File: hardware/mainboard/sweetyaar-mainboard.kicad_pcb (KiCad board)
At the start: 4 copper layers, 80 x 80 mm, 102 parts

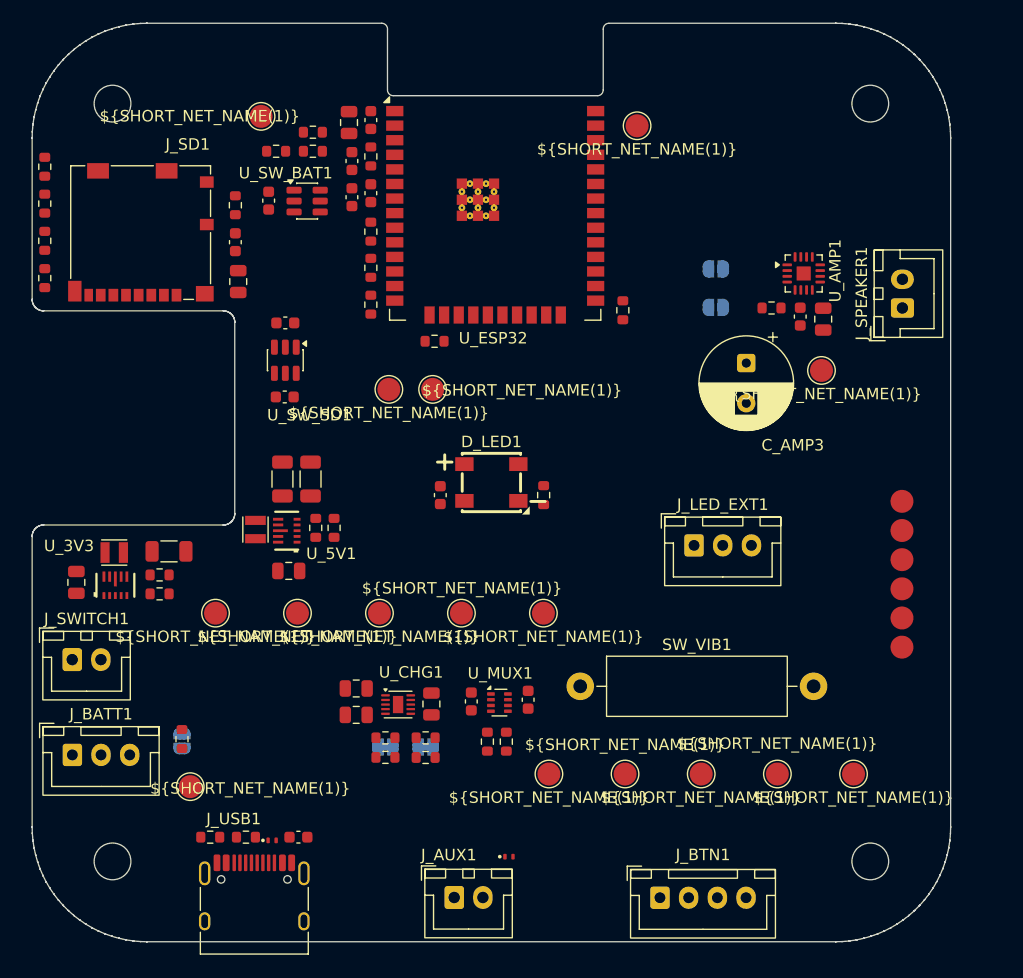
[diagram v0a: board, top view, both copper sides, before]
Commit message: Switch charger to firmware-supervised BQ25186
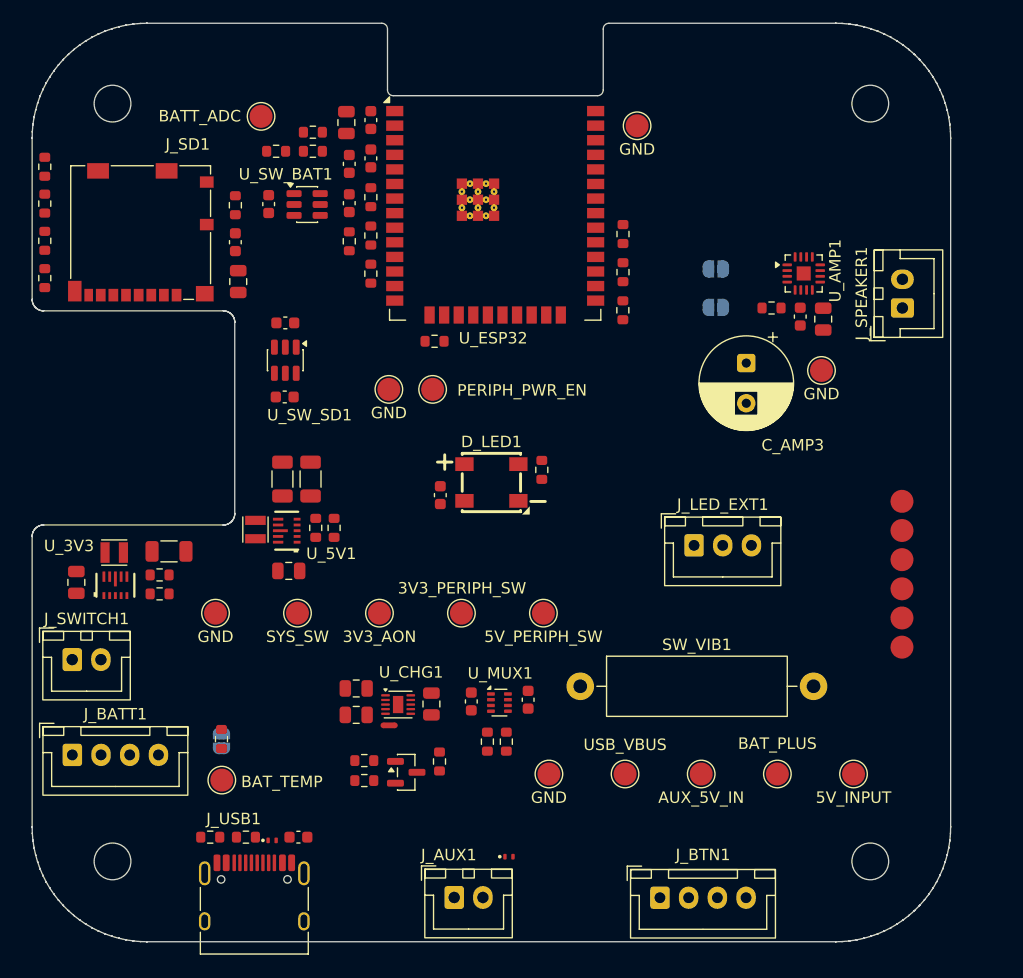
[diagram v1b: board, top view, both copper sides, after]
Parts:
- removed JP_ILIM1: JP_ILIM, Jumper:SolderJumper-2_P1.3mm_Bridged_RoundedPad1.0x1.5mm
- removed JP_ISET1: JP_ISET, Jumper:SolderJumper-2_P1.3mm_Bridged_RoundedPad1.0x1.5mm
- removed R_ILIM1: 5.1k, Resistor_SMD:R_0603_1608Metric
- removed R_ILIM2: 13k, Resistor_SMD:R_0603_1608Metric
- removed R_ISET1, R_ISET2: 301, Resistor_SMD:R_0603_1608Metric
- removed R_STAT1, R_STAT2: 10k, Resistor_SMD:R_0603_1608Metric
- added NT1: NetTie_2, NetTie:NetTie-2_SMD_Pad0.5mm, F.Cu at (51.1, 81.2)
- added Q1: MMBT3904, Package_TO_SOT_SMD:SOT-23, F.Cu at (52.6, 85.2)
- added R_CHARGER_CE_BASE1: 10k, Resistor_SMD:R_0603_1608Metric, F.Cu at (48.9, 84.2)
- added R_CHARGER_CE_PD1: 100k, Resistor_SMD:R_0603_1608Metric, F.Cu at (48.9, 86.0)
- added R_CHARGER_CE_PU1: 100k, Resistor_SMD:R_0603_1608Metric, F.Cu at (55.5, 84.3)
- added R_INT1: 10k, Resistor_SMD:R_0603_1608Metric, F.Cu at (49.5, 38.5)
- added R_PG1: 10k, Resistor_SMD:R_0603_1608Metric, F.Cu at (47.6, 39.0)
- added R_SCL1: 10k, Resistor_SMD:R_0603_1608Metric, F.Cu at (71.5, 38.4)
- added R_SDA1: 10k, Resistor_SMD:R_0603_1608Metric, F.Cu at (71.5, 41.7)
- J_BATT1: footprint Connector_JST:JST_XH_B3B-XH-A_1x03_P2.50mm_Vertical -> Connector_JST:JST_XH_B4B-XH-A_1x04_P2.50mm_Vertical
- TP1: value ${SHORT_NET_NAME(1)} -> USB_VBUS
- TP10: value ${SHORT_NET_NAME(1)} -> BATT_ADC
- TP11: value ${SHORT_NET_NAME(1)} -> BAT_TEMP
- TP12, TP13, TP14, TP15, TP16: value ${SHORT_NET_NAME(1)} -> GND
- TP2: value ${SHORT_NET_NAME(1)} -> AUX_5V_IN
- TP3: value ${SHORT_NET_NAME(1)} -> BAT_PLUS
- TP4: value ${SHORT_NET_NAME(1)} -> 5V_INPUT
- TP5: value ${SHORT_NET_NAME(1)} -> SYS_SW
- TP6: value ${SHORT_NET_NAME(1)} -> 5V_PERIPH_SW
- TP7: value ${SHORT_NET_NAME(1)} -> 3V3_PERIPH_SW
- TP8: value ${SHORT_NET_NAME(1)} -> 3V3_AON
- TP9: value ${SHORT_NET_NAME(1)} -> PERIPH_PWR_EN
- U_CHG1: value BQ25185DLHR -> BQ25186DLHR
- moved R_ESP_EN_PULLUP1 3.55 mm to (49.5, 35.1), turned to -90 degrees
- moved JP3 3.44 mm to (36.5, 82.5)
- moved R_TH1 3.44 mm to (36.5, 82.3)
- moved C_ESP_EN1 3.03 mm to (49.5, 31.8)
- moved TP11 2.81 mm to (36.5, 85.9)
- moved R_VIB1 2.70 mm to (49.5, 41.8)
- moved R_LED_DIN1 2.21 mm to (64.4, 58.9)
- moved C_BAT_SW_IN1 0.57 mm to (47.6, 35.7)
- moved C_BAT_ADC1 0.34 mm to (47.6, 32.2)
- moved U_SW_BAT1 0.30 mm to (44.0, 35.8)
- moved C_BAT_SW_OUT1 0.30 mm to (40.6, 35.8)
- moved C_ESP2 0.23 mm to (47.4, 28.6)
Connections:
- J_BATT1 pad 1: BAT_PLUS -> GND
- J_BATT1 pad 2: GND -> BAT_PLUS
- J_BATT1 pad 3: BAT_TEMP -> /TS_RETURN
- R_TH1 pad 2: GND -> /TS_RETURN
- U_CHG1 pad 3: /CHARGER_STAT2 -> /CHARGER_PG
- U_CHG1 pad 4: GND -> /CHARGER_CE_N
- U_CHG1 pad 7: /ILIM_VSET -> /I2C_SDA
- U_CHG1 pad 8: /ISET_NET -> /I2C_SCL
- U_CHG1 pad 9: /CHARGER_STAT1 -> /CHARGER_INT
- U_ESP32 pad 13: unconnected-(U_ESP32-IO14-Pad13) -> /CHARGER_ENABLE
- U_ESP32 pad 27: unconnected-(U_ESP32-IO16-Pad27) -> /I2C_SDA
- U_ESP32 pad 28: unconnected-(U_ESP32-IO17-Pad28) -> /I2C_SCL
- U_ESP32 pad 6: /CHARGER_STAT1 -> /CHARGER_PG
- U_ESP32 pad 7: /CHARGER_STAT2 -> /CHARGER_INT

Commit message: Adding routing to PCB design
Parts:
- removed C17: 10uF, 25V X5R/X7R, ±20%, Capacitor_SMD:C_0805_2012Metric
- removed C2: 22uF, 16 V, X5R/X7R, ±20%, Capacitor_SMD:C_1206_3216Metric
- removed TP12: GND, TestPoint:TestPoint_Pad_D2.0mm
- added C_3V3_OUT1: 22uF, 16 V, X5R/X7R, ±20%, Capacitor_SMD:C_1206_3216Metric, F.Cu at (31.1, 66.1)
- added C_5V_IN1: 10uF, 25V X5R/X7R, ±20%, Capacitor_SMD:C_0805_2012Metric, F.Cu at (48.2, 67.3)
- added C_MUX4: 1uF, 25 V, X7R, ±10%, Capacitor_SMD:C_0603_1608Metric, F.Cu at (52.7, 86.1)
- added LOGO: Logo_SweetYaar_Teddy_20x20mm, SweetYaar:Logo_SweetYaar_Teddy_20x20mm, F.Cu at (80.8, 83.5)
- moved TP3 46.5 mm to (38.5, 82.5)
- moved TP4 30.7 mm to (60.8, 85.4)
- moved TP15 18.4 mm to (69.4, 51.5)
- moved C_3V3_IN1 18.3 mm to (24.1, 69.0), turned to -90 degrees
- moved C_MUX1 14.7 mm to (46.6, 88.0), turned to 180 degrees
- moved C_MUX2 13.8 mm to (52.7, 87.9), turned to 0 degrees
- moved U_MUX1 13.8 mm to (49.6, 87.4)
- moved R_PR1_BOT1 13.1 mm to (50.2, 91.6)
- moved R_PR1_TOP1 13.1 mm to (51.8, 91.6)
- moved TP2 11.8 mm to (67.1, 89.4)
- moved TP1 11.5 mm to (60.8, 89.4)
- moved R_CHARGER_CE_PU1 10.6 mm to (64.4, 78.6)
- moved Q1 10.6 mm to (61.5, 79.5)
- moved R_CHARGER_CE_BASE1 10.6 mm to (57.9, 78.5)
- moved R_CHARGER_CE_PD1 10.6 mm to (57.9, 80.2)
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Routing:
- net GND: track 0.00 -> 136.3 mm, vias 0 -> 54
- net 3V3_AON: track 0.00 -> 117.7 mm, vias 0 -> 24
- net /ESP_EN: track 0.00 -> 106.4 mm, vias 0 -> 4
- net /BTN_SONG: track 0.00 -> 94.3 mm, vias 0 -> 2
- net /BTN_ANIMAL: track 0.00 -> 93.5 mm, vias 0 -> 2
- net BAT_PLUS: track 0.00 -> 87.3 mm, vias 0 -> 2
- net /UART_TXD: track 0.00 -> 84.2 mm
- net /UART_RXD: track 0.00 -> 79.3 mm
- net 3V3_PERIPH_SW: track 0.00 -> 70.9 mm, vias 0 -> 11
- net /SD_MOSI: track 0.00 -> 69.5 mm, vias 0 -> 4
- net /CHARGER_PG: track 0.00 -> 69.2 mm, vias 0 -> 2
- net /SD_CS: track 0.00 -> 68.8 mm, vias 0 -> 2
- net /BOOT: track 0.00 -> 67.7 mm
- net /SD_MISO: track 0.00 -> 65.2 mm, vias 0 -> 2
- net /SD_CLK: track 0.00 -> 59.7 mm, vias 0 -> 2
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- added copper zone on F.Cu, net /5V_INPUT
- added copper zone on F.Cu, net /SYS
- added copper zone on F.Cu, net /SYS_SW
- added copper zone on B.Cu, net 3V3_AON
- added copper zone on F.Cu, net 3V3_AON
- added copper zone on B.Cu, net 3V3_PERIPH_SW
- added copper zone on B.Cu, net 5V_PERIPH_SW
- added copper zone on F.Cu, net 5V_PERIPH_SW
- added copper zone on F.Cu, net BAT_PLUS
- added copper zone on F.Cu, net GND
- added copper zone on In1.Cu, net GND
- added copper zone on In2.Cu, net GND
- added copper zone on F.Cu, net Net-(U_3V3-L1)
- added copper zone on F.Cu, net Net-(U_3V3-L2)
- added copper zone on F.Cu, net Net-(U_5V1-L1)
- added copper zone on F.Cu, net Net-(U_5V1-L2)
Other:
- board text added: "Built with love by Zach Moshe for the world's cutest child ♥, 2022. Reimagined with Codex & Claude, 2026."
- board text added: "Close the jumper if no thermistor is connected to the battery harness. This connects a 10k resistor instead which the charger reads as a normal temperature."
- board text added: "High volume (12 dB)"
- board text added: "If both jumpers are open, volume is at a default level (9 dB). Close one of the jumpers to change settings. IMPORTANT: NEVER CLOSE BOTH!"
- board text added: "J_PROG1"
- board text added: "Low volume (6 dB)"

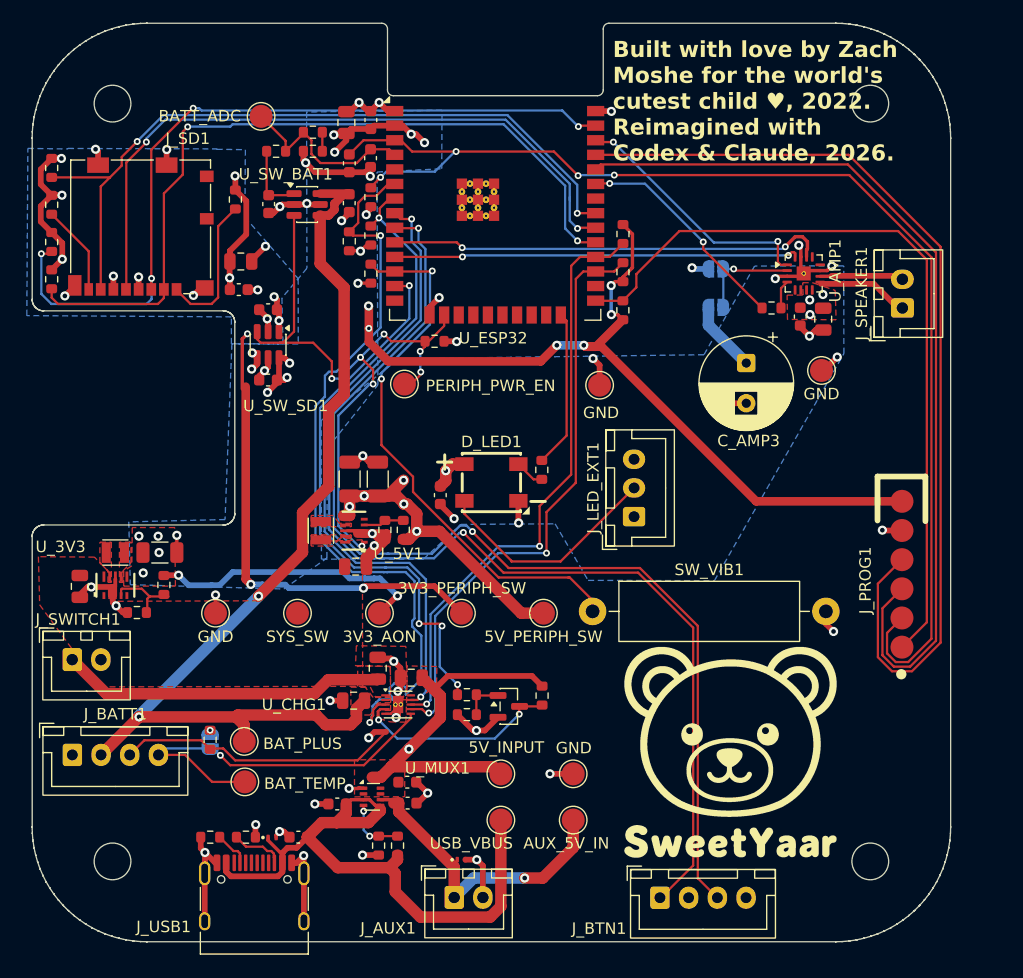
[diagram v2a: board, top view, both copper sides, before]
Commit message: Adding QR codes for repo and app; Adding version number to the silkscreen
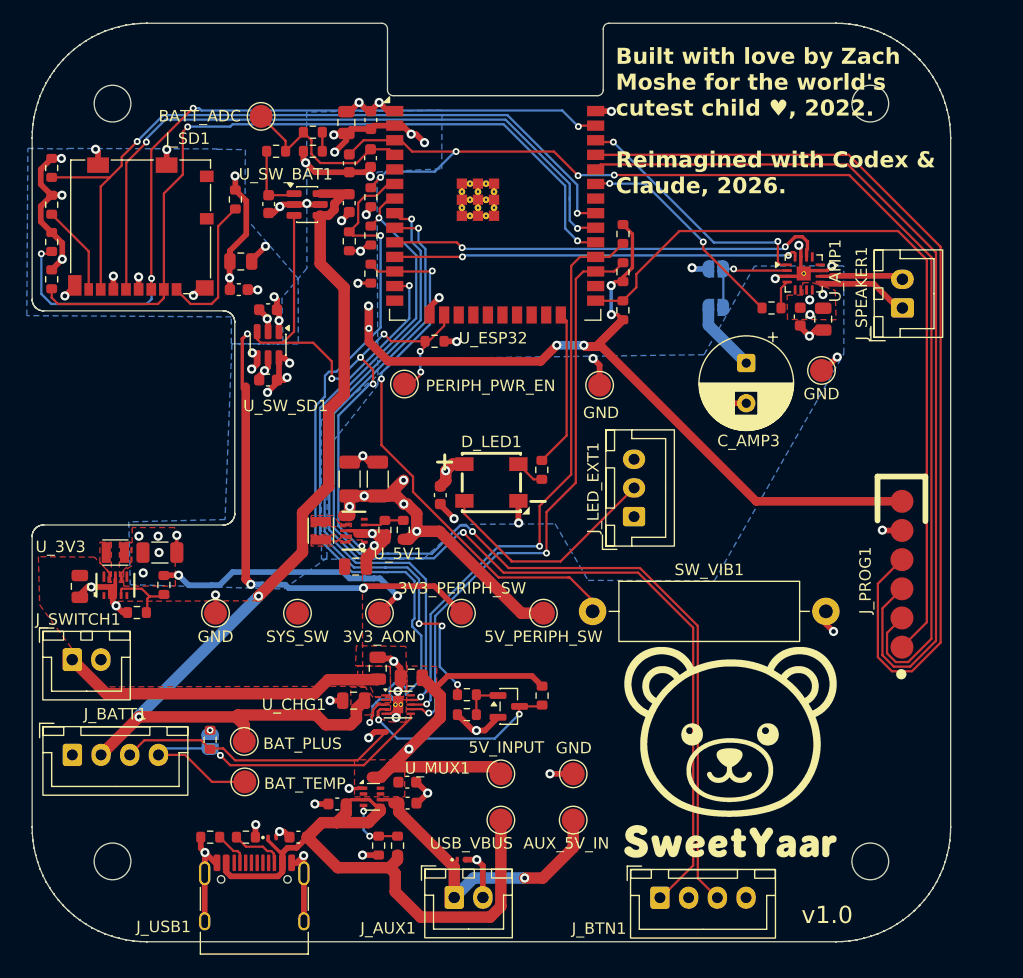
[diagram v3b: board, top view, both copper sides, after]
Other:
- board text added: "App"
- board text added: "Repo"
- board text added: "v1.0"

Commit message: Moving LED to the edge of the board
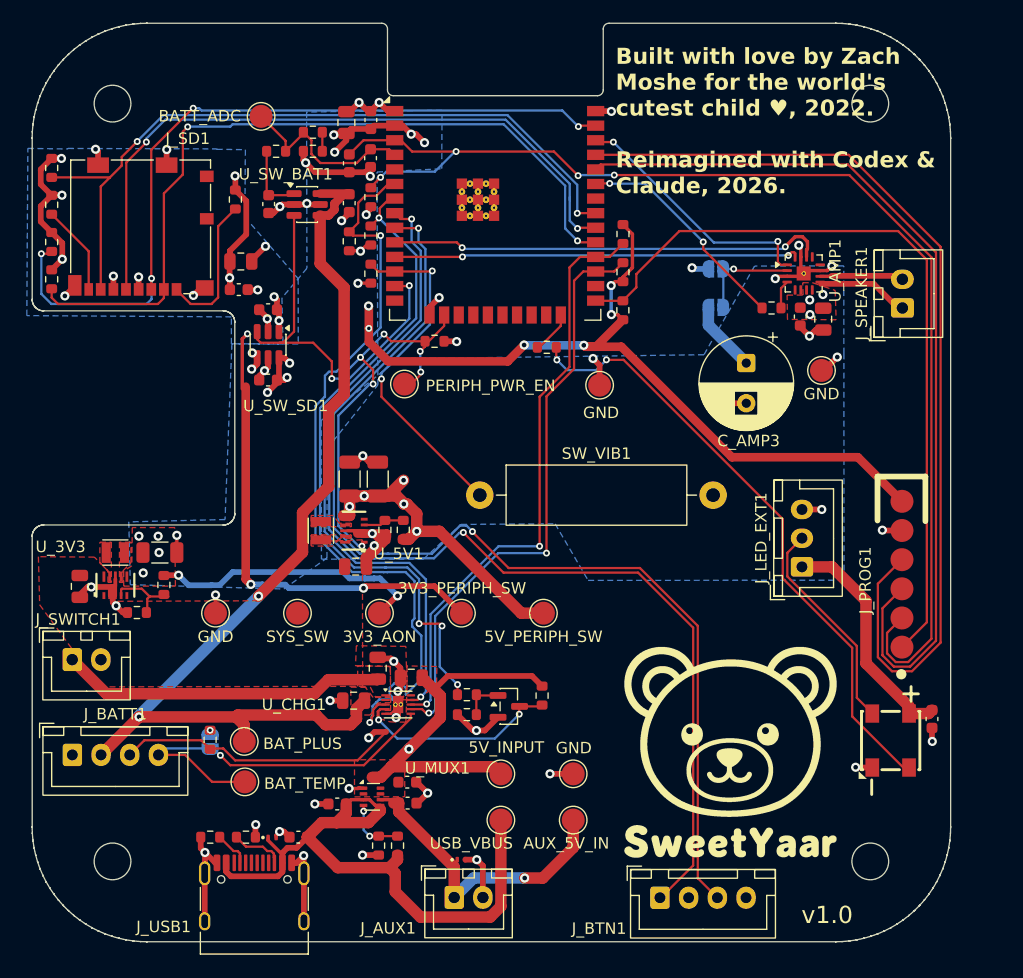
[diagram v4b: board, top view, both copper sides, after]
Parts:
- R_LED_DIN1: value 301 -> 330
- moved C_LED1 47.1 mm to (98.4, 80.6)
- moved D_LED1 41.4 mm to (94.8, 82.5), turned to -90 degrees
- moved J_LED_EXT1 15.3 mm to (87.0, 67.3)
- moved SW_VIB1 14.1 mm to (59.0, 61.1)
- moved R_LED_DIN1 10.7 mm to (64.8, 48.2), turned to 180 degrees
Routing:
- net Net-(D_LED1-DIN): track 2.59 -> 53.8 mm, vias 0 -> 2
- net /VIB_WAKE: track 48.4 -> 30.5 mm
- net 5V_PERIPH_SW: track 38.2 -> 55.1 mm, vias 9 -> 8
- net /STATUS_LED_GPIO: track 13.8 -> 4.27 mm
- net Net-(D_LED1-DOUT): track 20.3 -> 18.9 mm
- net GND: track 136.3 -> 134.9 mm

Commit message: Fixing rotation and position offsets
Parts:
- J_USB1: footprint SweetYaar:USB_C_Receptacle_HRO_TYPE-C-31-M-12 -> SweetYaar:USB_C_Receptacle_HRO_TYPE-C-31-M-12 - C165948
- U_AMP1: footprint SweetYaar:TQFN-16-1EP_3x3mm_P0.5mm_EP1.23x1.23mm -> SweetYaar:TQFN-16-1EP_3x3mm_P0.5mm_EP1.23x1.23mm - C910544
- U_ESP32: footprint RF_Module:ESP32-WROOM-32E -> SweetYaar:ESP32-WROOM-32E - C701342
- U_MUX1: footprint Package_TO_SOT_SMD:SOT-583-8 -> SweetYaar:SOT-583-8 - C3235557
- U_SW_BAT1, U_SW_SD1: footprint Package_TO_SOT_SMD:SOT-23-6 -> SweetYaar:SOT-23-6 - C128634

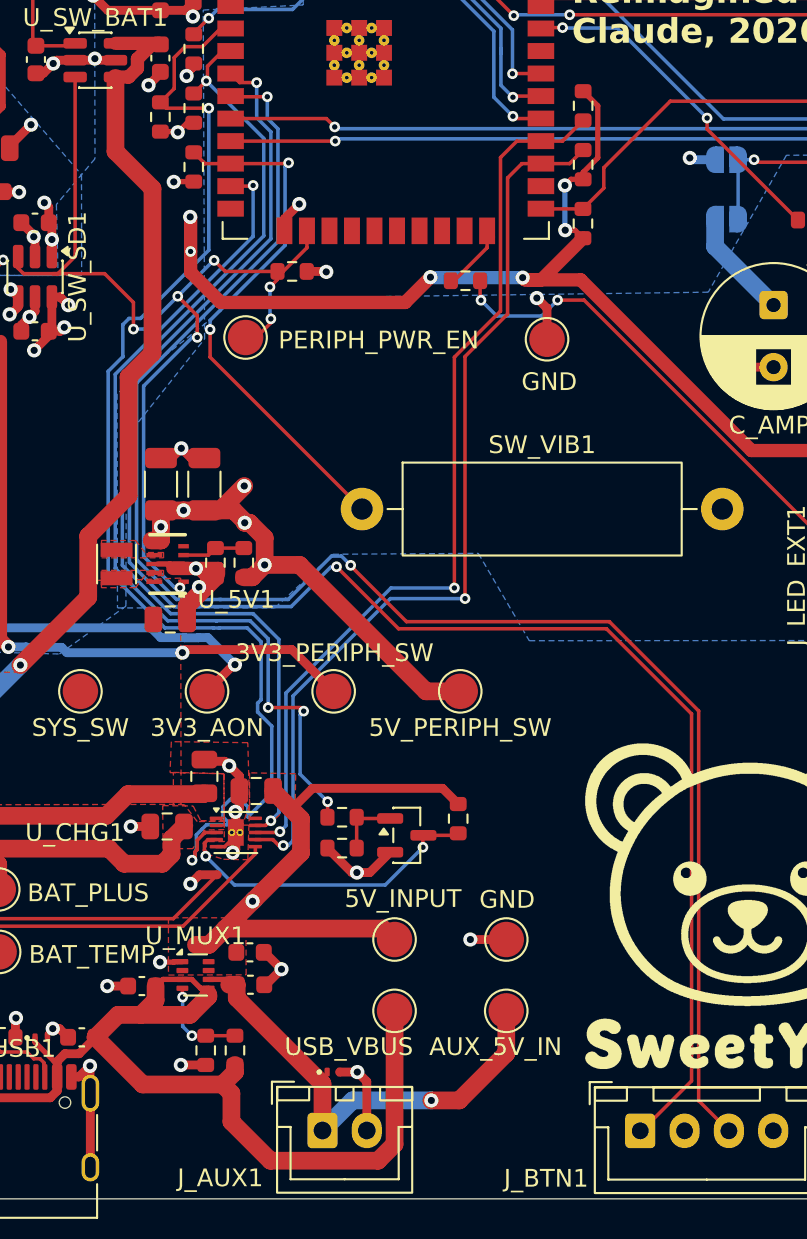
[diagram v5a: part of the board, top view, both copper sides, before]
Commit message: minor routing changes
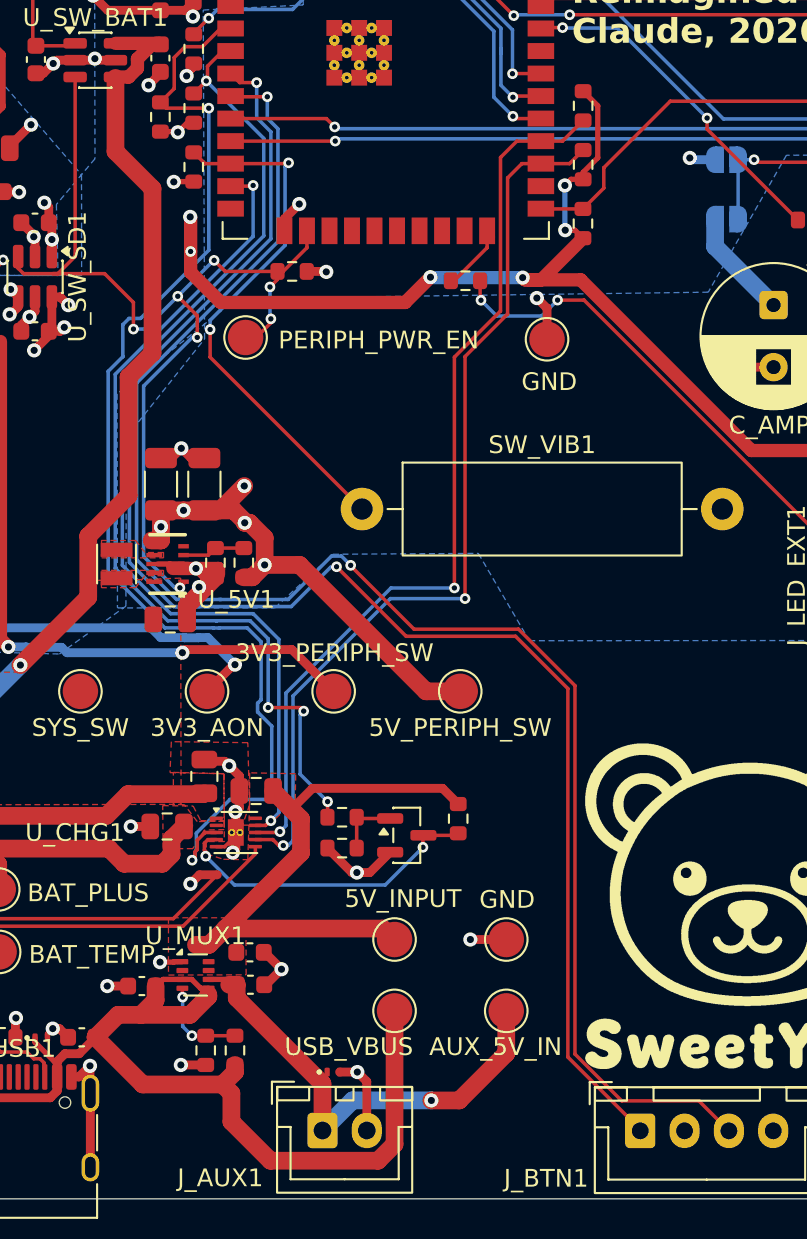
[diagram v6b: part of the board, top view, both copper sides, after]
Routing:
- net /BTN_SONG: track 94.3 -> 88.8 mm
- net /CHARGER_PG: track 69.2 -> 67.0 mm
- net /BTN_ANIMAL: track 93.5 -> 92.8 mm
- net /5V_INPUT: track 32.4 -> 32.2 mm, vias 1 -> 0
